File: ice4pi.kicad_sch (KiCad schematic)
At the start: 34 parts, among them J1 Conn_02x03, J2 Raspberry_Pi_2_3, J3 USB_C_Receptacle_USB2.0, J4 RJ45_Abracon_ARJP11A-MASA-B-A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, U1 ENC28J60x-SS, U2 DSC1001DE1-025.0000, U3 TPS2375-1

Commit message: todo: fix led polarity
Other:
- note added: "TODO: FIX LED POLARITY"
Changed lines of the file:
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@@
+		)
+	)
+	(text "TODO: FIX LED POLARITY"
+		(exclude_from_sim no)
+		(at 105.41 88.9 0)
+		(effects
+			(font
+				(size 2.54 2.54)
+				(color 241 0 0 1)
+			)
 		)
 	)

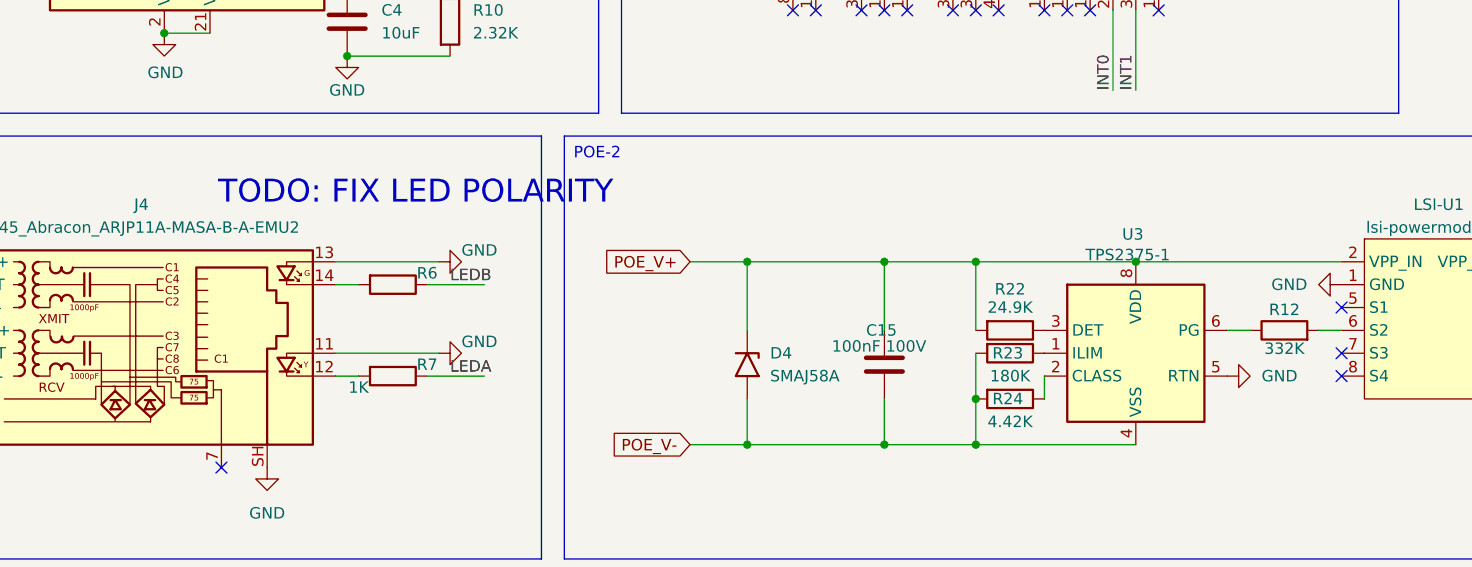
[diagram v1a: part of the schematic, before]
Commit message: fix: powergood is an open drain
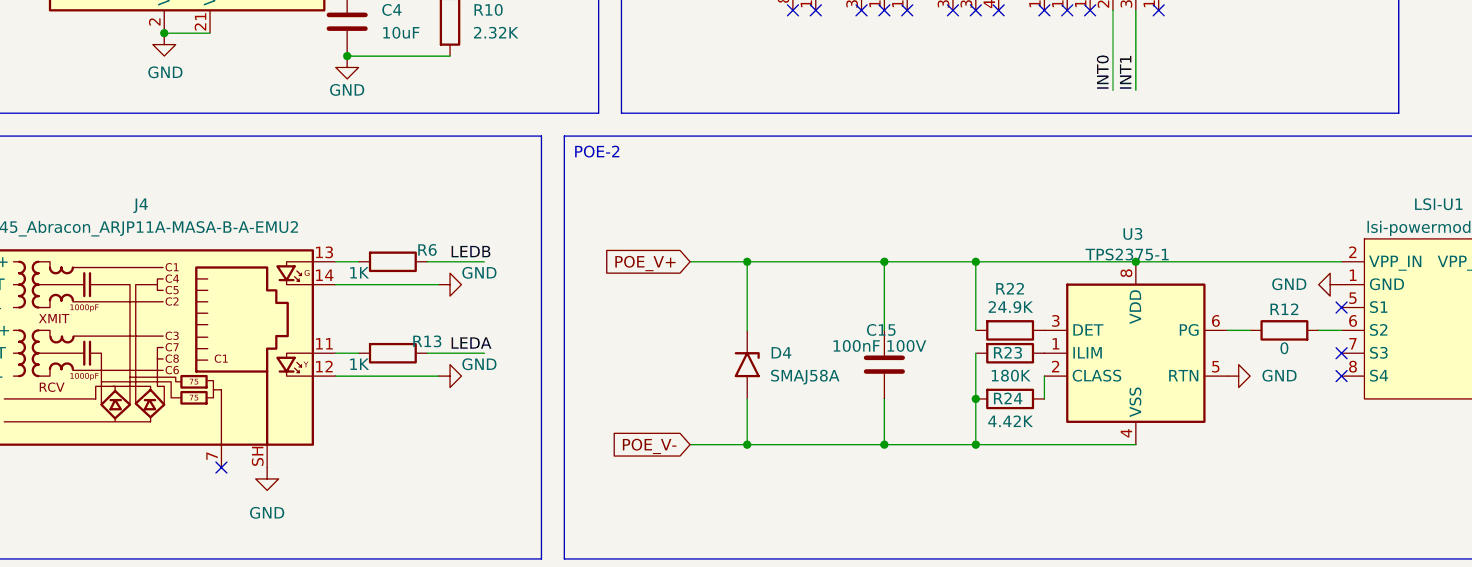
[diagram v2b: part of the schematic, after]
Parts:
- removed R7: 1K, Resistor_SMD:R_0402_1005Metric, symbol Device:R
- added R13: 1K, Resistor_SMD:R_0402_1005Metric, symbol Device:R
- R12: value 332K -> 0
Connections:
- net GND: now also J4.12, J4.14; no longer J4.11, J4.13
- net LEDA: now also R13.1
- net at R6.2: now also J4.13; no longer J4.14
- new net: J4.11, R13.2
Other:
- note removed: "TODO: FIX LED POLARITY"

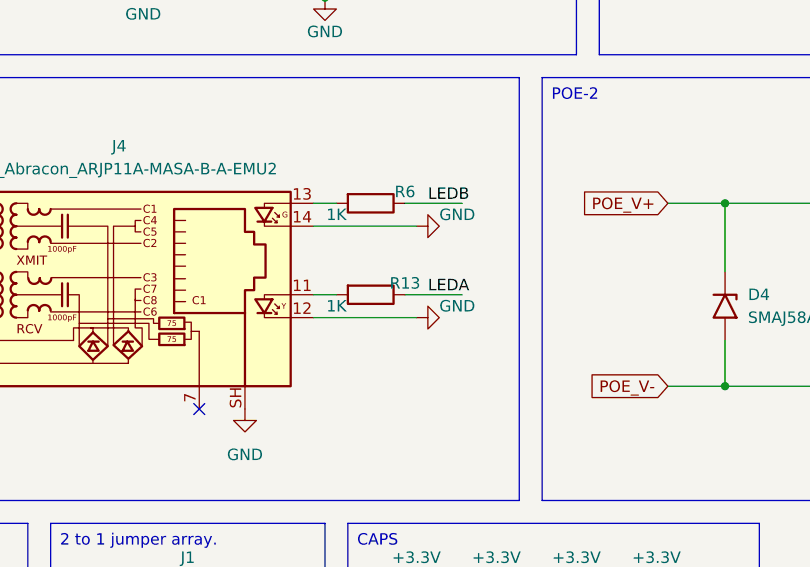
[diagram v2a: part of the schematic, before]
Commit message: feat: fixed led polarity
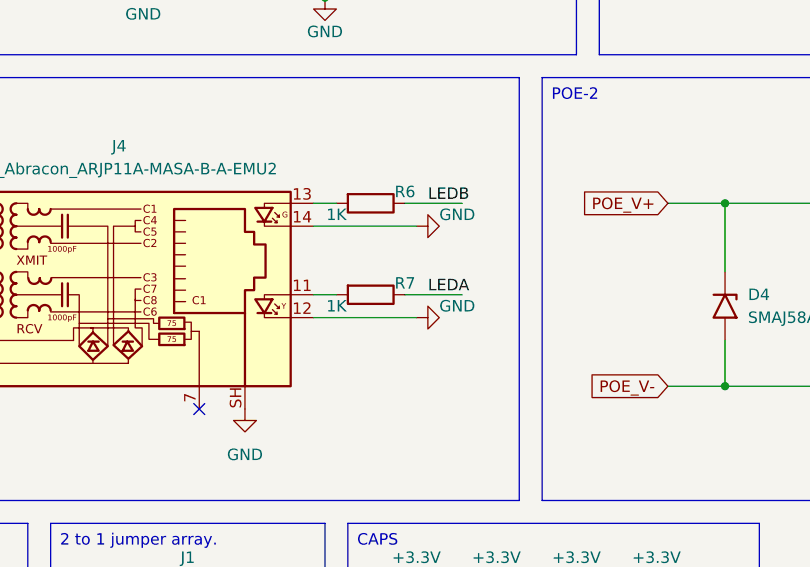
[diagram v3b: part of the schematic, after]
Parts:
- renumbered R13 to R7
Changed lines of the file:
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@@
 		(on_board yes)
 		(dnp no)
-		(property "Reference" "R13"
+		(property "Reference" "R7"
 			(at 106.68 105.41 90)
 			(effects
@@
 			(project "ice4pi"
 				(path "/0f54db53-a272-4955-88fb-d7ab00657bb0"
-					(reference "R13")
+					(reference "R7")
 					(unit 1)
 				)
